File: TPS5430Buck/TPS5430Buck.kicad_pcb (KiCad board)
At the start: 2 copper layers, 61 x 28 mm, 15 parts, among them J11 Screw_Terminal_01x02, J12 Conn_01x03_Pin, U3 TPS5430DDA

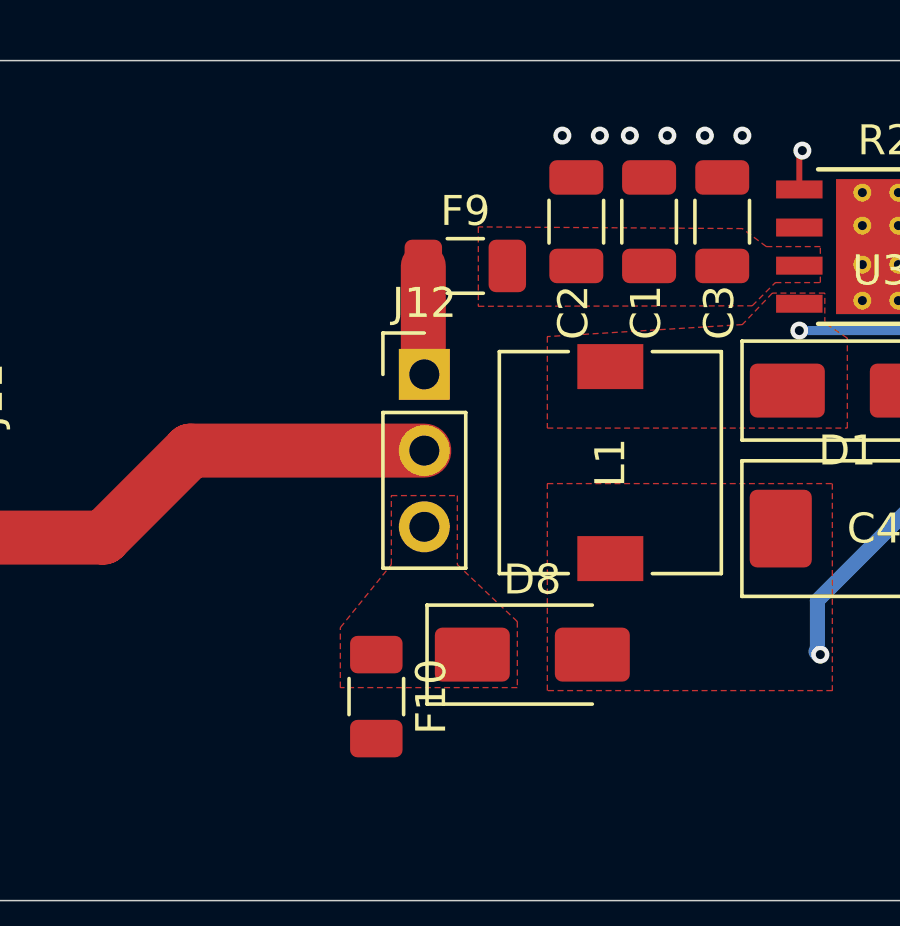
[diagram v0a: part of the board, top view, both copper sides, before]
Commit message: TPS5430Buck: fuse re-annotation (F10->F8, F9->F7) and project settings rewritten by newer KiCad
Uncommitted state carried over from the former TPS5430Buck repo.

Co-Authored-By: Claude Opus 5.5 <noreply@anthropic.com>
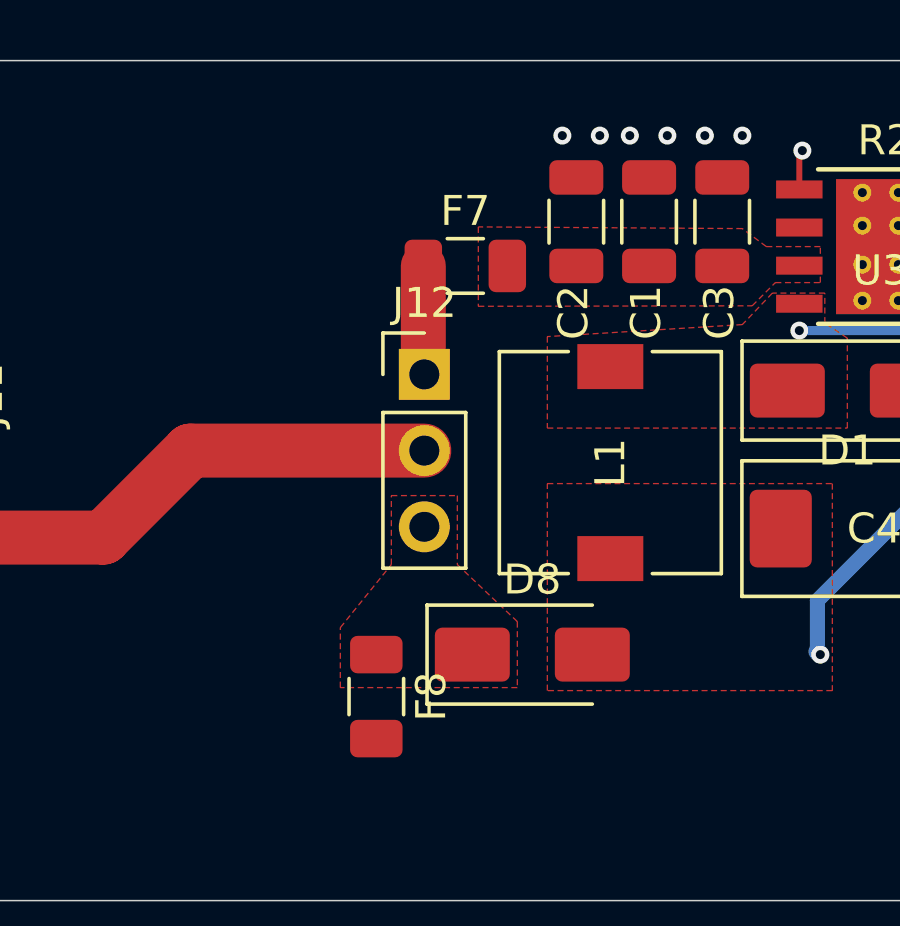
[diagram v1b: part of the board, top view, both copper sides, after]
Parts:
- renumbered F9 to F7, F10 to F8
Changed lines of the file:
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@@
 		(descr "Fuse SMD 1206 (3216 Metric), square (rectangular) end terminal, IPC-7351 nominal, (Body size source: http://www.tortai-tech.com/upload/download/2011102023233369053.pdf)")
 		(tags "fuse")
-		(property "Reference" "F10"
+		(property "Reference" "F8"
 			(at 0 -1.83 90)
 			(layer "F.SilkS")
@@
 		(descr "Fuse SMD 1206 (3216 Metric), square (rectangular) end terminal, IPC-7351 nominal, (Body size source: http://www.tortai-tech.com/upload/download/2011102023233369053.pdf)")
 		(tags "fuse")
-		(property "Reference" "F9"
+		(property "Reference" "F7"
 			(at 0 -1.83 0)
 			(layer "F.SilkS")
